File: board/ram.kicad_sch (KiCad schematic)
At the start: 8 parts, among them U1 RAM 1 LO, U5 RAM 2 LO, U6 RAM 1 LO, U7 RAM 2 LO

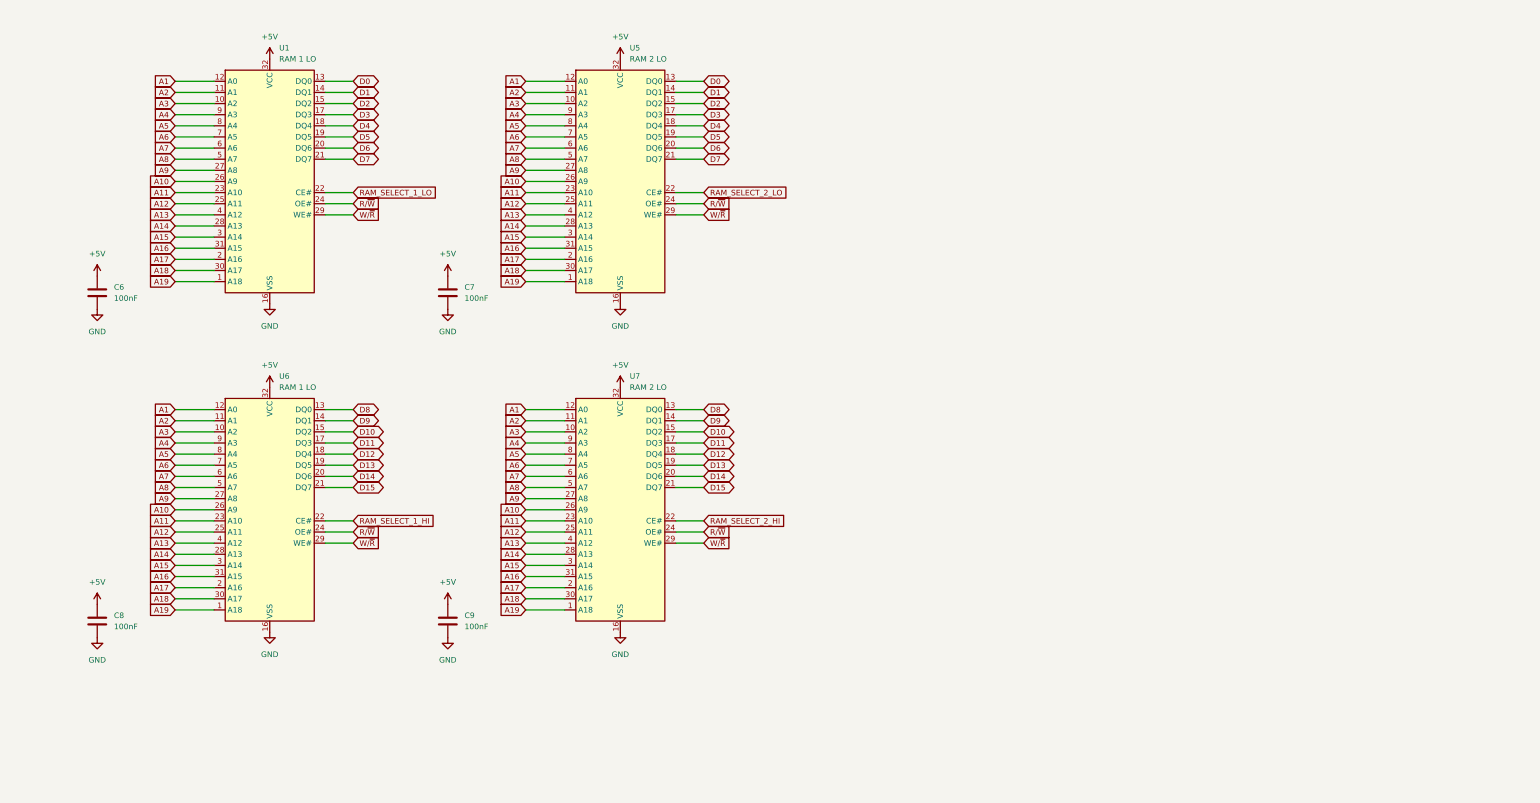
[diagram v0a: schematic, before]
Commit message: fill out most functionality - passes ERC
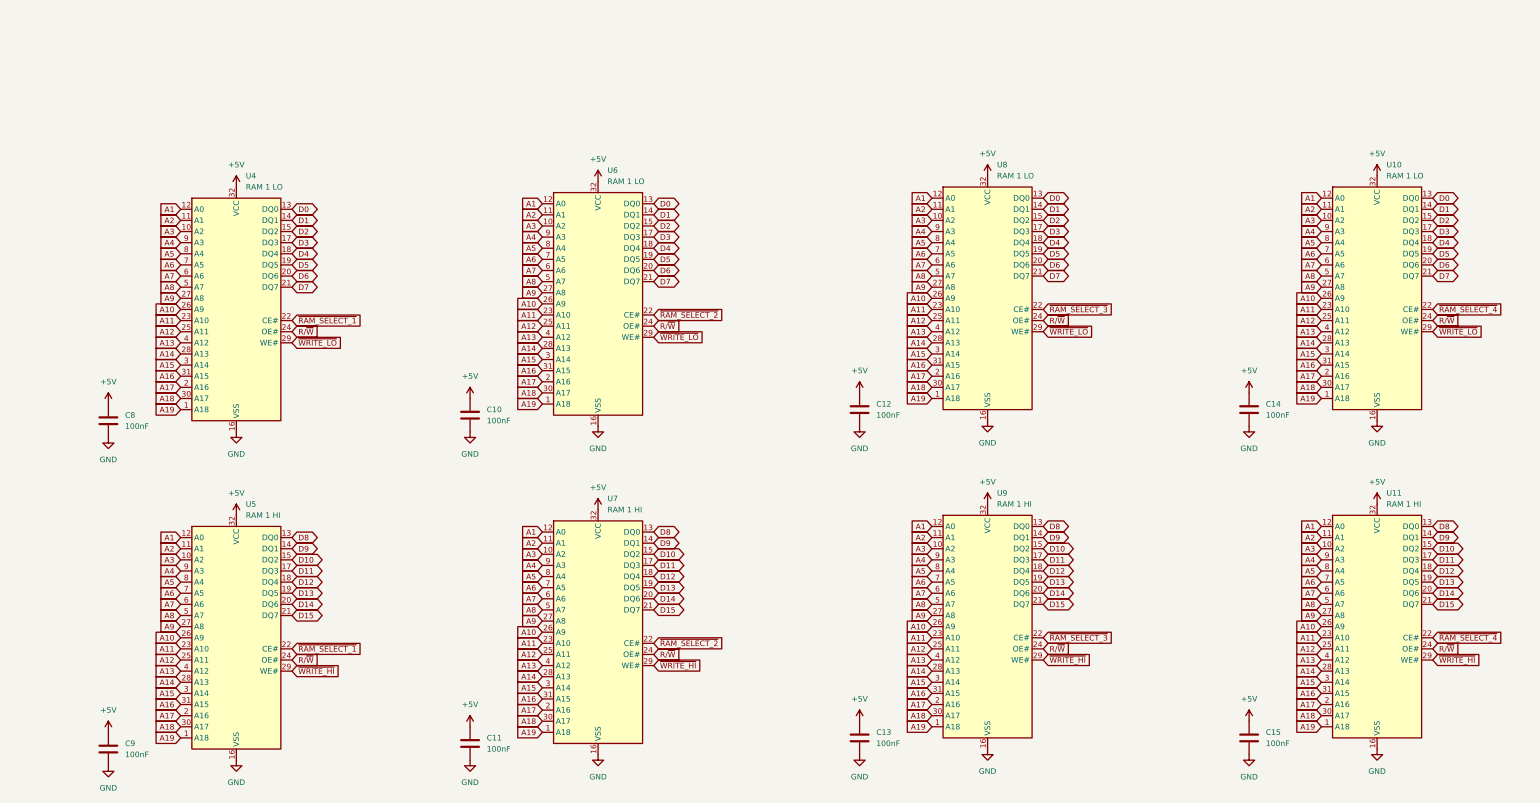
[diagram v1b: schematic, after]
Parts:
- removed C6, C7, C9: 100nF, symbol Device:C
- removed U5: RAM 2 LO, Package_DIP:DIP-32_W15.24mm, symbol Memory_RAM:AS6C4008-55PCN
- added C10, C11, C12, C13, C14, C15, C8: 100nF, symbol Device:C
- added U10, U6, U8: RAM 1 LO, Package_DIP:DIP-32_W15.24mm, symbol Memory_RAM:AS6C4008-55PCN
- added U11, U9: RAM 1 HI, Package_DIP:DIP-32_W15.24mm, symbol Memory_RAM:AS6C4008-55PCN
- U5: renamed from U6; value RAM 1 LO -> RAM 1 HI
- U7: value RAM 2 LO -> RAM 1 HI
- renumbered C8 to C9, U1 to U4
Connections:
- net RAM_SELECT_1_LO is gone; now on net ~{RAM_SELECT_1}: U4.22 (CE#)
- net +5V: now also C10.1, C11.1, C12.1, C13.1, C14.1, C15.1, C8.1, U10.32 (VCC), U11.32 (VCC), U6.32 (VCC), U8.32 (VCC), U9.32 (VCC)
- net A1: now also U10.12 (A0), U11.12 (A0), U6.12 (A0), U8.12 (A0), U9.12 (A0)
- net A10: now also U10.26 (A9), U11.26 (A9), U6.26 (A9), U8.26 (A9), U9.26 (A9)
- net A11: now also U10.23 (A10), U11.23 (A10), U6.23 (A10), U8.23 (A10), U9.23 (A10)
- net A12: now also U10.25 (A11), U11.25 (A11), U6.25 (A11), U8.25 (A11), U9.25 (A11)
- net A13: now also U10.4 (A12), U11.4 (A12), U6.4 (A12), U8.4 (A12), U9.4 (A12)
- net A14: now also U10.28 (A13), U11.28 (A13), U6.28 (A13), U8.28 (A13), U9.28 (A13)
- net A15: now also U10.3 (A14), U11.3 (A14), U6.3 (A14), U8.3 (A14), U9.3 (A14)
- net A16: now also U10.31 (A15), U11.31 (A15), U6.31 (A15), U8.31 (A15), U9.31 (A15)
- net A17: now also U10.2 (A16), U11.2 (A16), U6.2 (A16), U8.2 (A16), U9.2 (A16)
- net A18: now also U10.30 (A17), U11.30 (A17), U6.30 (A17), U8.30 (A17), U9.30 (A17)
- net A19: now also U10.1 (A18), U11.1 (A18), U6.1 (A18), U8.1 (A18), U9.1 (A18)
- net A2: now also U10.11 (A1), U11.11 (A1), U6.11 (A1), U8.11 (A1), U9.11 (A1)
- net A3: now also U10.10 (A2), U11.10 (A2), U6.10 (A2), U8.10 (A2), U9.10 (A2)
- net A4: now also U10.9 (A3), U11.9 (A3), U6.9 (A3), U8.9 (A3), U9.9 (A3)
- net A5: now also U10.8 (A4), U11.8 (A4), U6.8 (A4), U8.8 (A4), U9.8 (A4)
- net A6: now also U10.7 (A5), U11.7 (A5), U6.7 (A5), U8.7 (A5), U9.7 (A5)
- net A7: now also U10.6 (A6), U11.6 (A6), U6.6 (A6), U8.6 (A6), U9.6 (A6)
- net A8: now also U10.5 (A7), U11.5 (A7), U6.5 (A7), U8.5 (A7), U9.5 (A7)
- net A9: now also U10.27 (A8), U11.27 (A8), U6.27 (A8), U8.27 (A8), U9.27 (A8)
- net D0: now also U10.13 (DQ0), U6.13 (DQ0), U8.13 (DQ0)
- net D1: now also U10.14 (DQ1), U6.14 (DQ1), U8.14 (DQ1)
- net D10: now also U11.15 (DQ2), U9.15 (DQ2)
- net D11: now also U11.17 (DQ3), U9.17 (DQ3)
- net D12: now also U11.18 (DQ4), U9.18 (DQ4)
- net D13: now also U11.19 (DQ5), U9.19 (DQ5)
- net D14: now also U11.20 (DQ6), U9.20 (DQ6)
- net D15: now also U11.21 (DQ7), U9.21 (DQ7)
- net D2: now also U10.15 (DQ2), U6.15 (DQ2), U8.15 (DQ2)
- net D3: now also U10.17 (DQ3), U6.17 (DQ3), U8.17 (DQ3)
- net D4: now also U10.18 (DQ4), U6.18 (DQ4), U8.18 (DQ4)
- net D5: now also U10.19 (DQ5), U6.19 (DQ5), U8.19 (DQ5)
- net D6: now also U10.20 (DQ6), U6.20 (DQ6), U8.20 (DQ6)
- net D7: now also U10.21 (DQ7), U6.21 (DQ7), U8.21 (DQ7)
- net D8: now also U11.13 (DQ0), U9.13 (DQ0)
- net D9: now also U11.14 (DQ1), U9.14 (DQ1)
- net GND: now also C10.2, C11.2, C12.2, C13.2, C14.2, C15.2, C8.2, U10.16 (VSS), U11.16 (VSS), U6.16 (VSS), U8.16 (VSS), U9.16 (VSS)
- net R/~{W}: now also U10.24 (OE#), U11.24 (OE#), U6.24 (OE#), U8.24 (OE#), U9.24 (OE#)
- net RAM_SELECT_1_HI renamed ~{RAM_SELECT_1}
- net RAM_SELECT_2_HI renamed ~{RAM_SELECT_2}
- net ~{RAM_SELECT_2}: now also U6.22 (CE#)
- net W/~{R} renamed ~{WRITE_HI}
- net ~{WRITE_HI}: now also U11.29 (WE#), U9.29 (WE#); no longer U4.29 (WE#)
- new net ~{RAM_SELECT_3}: U8.22 (CE#), U9.22 (CE#)
- new net ~{RAM_SELECT_4}: U10.22 (CE#), U11.22 (CE#)
- new net ~{WRITE_LO}: U10.29 (WE#), U4.29 (WE#), U6.29 (WE#), U8.29 (WE#)
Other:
- moved on the sheet: C9, U4, U5

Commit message: design draft complete, added footprints
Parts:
- C10, C11, C12, C13, C14, C15, C8, C9: footprint (none) -> Capacitor_THT:C_Disc_D5.0mm_W2.5mm_P5.00mm
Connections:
- net R/~{W} renamed ~{R}/W
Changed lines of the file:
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@@
 		)
 	)
-	(global_label "R{slash}~{W}"
+	(global_label "~{R}{slash}W"
 		(shape input)
 		(at 250.19 165.1 0)
@@
 		)
 	)
-	(global_label "R{slash}~{W}"
+	(global_label "~{R}{slash}W"
 		(shape input)
 		(at 161.29 166.37 0)
@@
 		)
 	)
-	(global_label "R{slash}~{W}"
+	(global_label "~{R}{slash}W"
 		(shape input)
 		(at 339.09 90.17 0)
@@
 		)
 	)
-	(global_label "R{slash}~{W}"
+	(global_label "~{R}{slash}W"
 		(shape input)
 		(at 250.19 90.17 0)
@@
 		)
 	)
-	(global_label "R{slash}~{W}"
+	(global_label "~{R}{slash}W"
 		(shape input)
 		(at 161.29 91.44 0)
@@
 		)
 	)
-	(global_label "R{slash}~{W}"
+	(global_label "~{R}{slash}W"
 		(shape input)
 		(at 339.09 165.1 0)
@@
 		)
 	)
-	(global_label "R{slash}~{W}"
+	(global_label "~{R}{slash}W"
 		(shape input)
 		(at 78.74 92.71 0)
@@
 		)
 	)
-	(global_label "R{slash}~{W}"
+	(global_label "~{R}{slash}W"
 		(shape input)
 		(at 78.74 167.64 0)
@@
 			)
 		)
-		(property "Footprint" ""
+		(property "Footprint" "Capacitor_THT:C_Disc_D5.0mm_W2.5mm_P5.00mm"
 			(at 120.3452 190.5 0)
 			(effects
@@
 			)
 		)
-		(property "Footprint" ""
+		(property "Footprint" "Capacitor_THT:C_Disc_D5.0mm_W2.5mm_P5.00mm"
 			(at 298.1452 189.23 0)
 			(effects
@@
 			)
 		)
-		(property "Footprint" ""
+		(property "Footprint" "Capacitor_THT:C_Disc_D5.0mm_W2.5mm_P5.00mm"
 			(at 120.3452 115.57 0)
 			(effects
@@
 			)
 		)
-		(property "Footprint" ""
+		(property "Footprint" "Capacitor_THT:C_Disc_D5.0mm_W2.5mm_P5.00mm"
 			(at 37.7952 116.84 0)
 			(effects
@@
 			)
 		)
-		(property "Footprint" ""
+		(property "Footprint" "Capacitor_THT:C_Disc_D5.0mm_W2.5mm_P5.00mm"
 			(at 37.7952 191.77 0)
 			(effects
@@
 			)
 		)
-		(property "Footprint" ""
+		(property "Footprint" "Capacitor_THT:C_Disc_D5.0mm_W2.5mm_P5.00mm"
 			(at 298.1452 114.3 0)
 			(effects
@@
 			)
 		)
-		(property "Footprint" ""
+		(property "Footprint" "Capacitor_THT:C_Disc_D5.0mm_W2.5mm_P5.00mm"
 			(at 209.2452 189.23 0)
 			(effects
@@
 			)
 		)
-		(property "Footprint" ""
+		(property "Footprint" "Capacitor_THT:C_Disc_D5.0mm_W2.5mm_P5.00mm"
 			(at 209.2452 114.3 0)
 			(effects

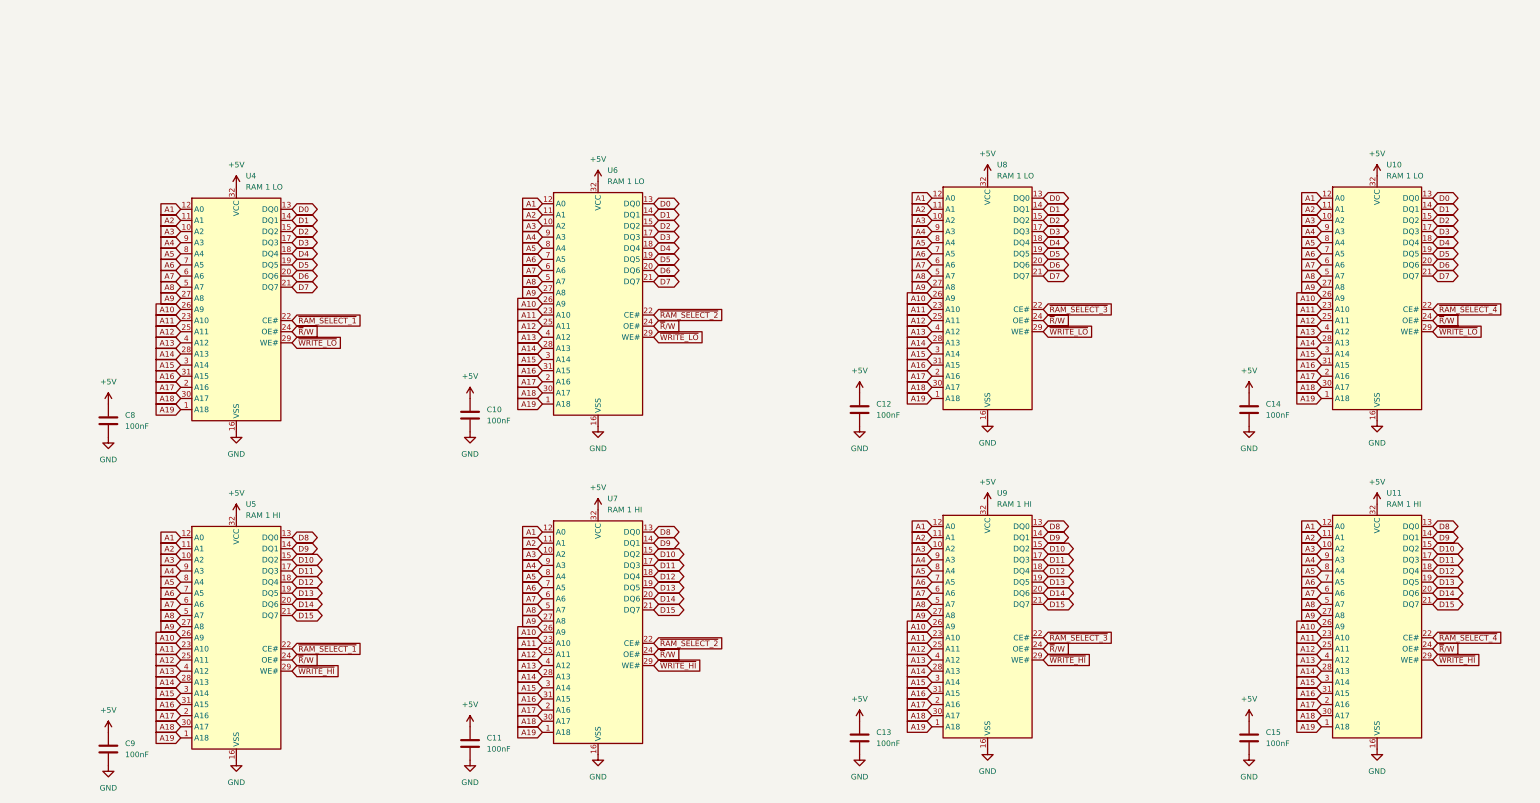
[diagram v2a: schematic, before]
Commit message: start of PCB and MMU
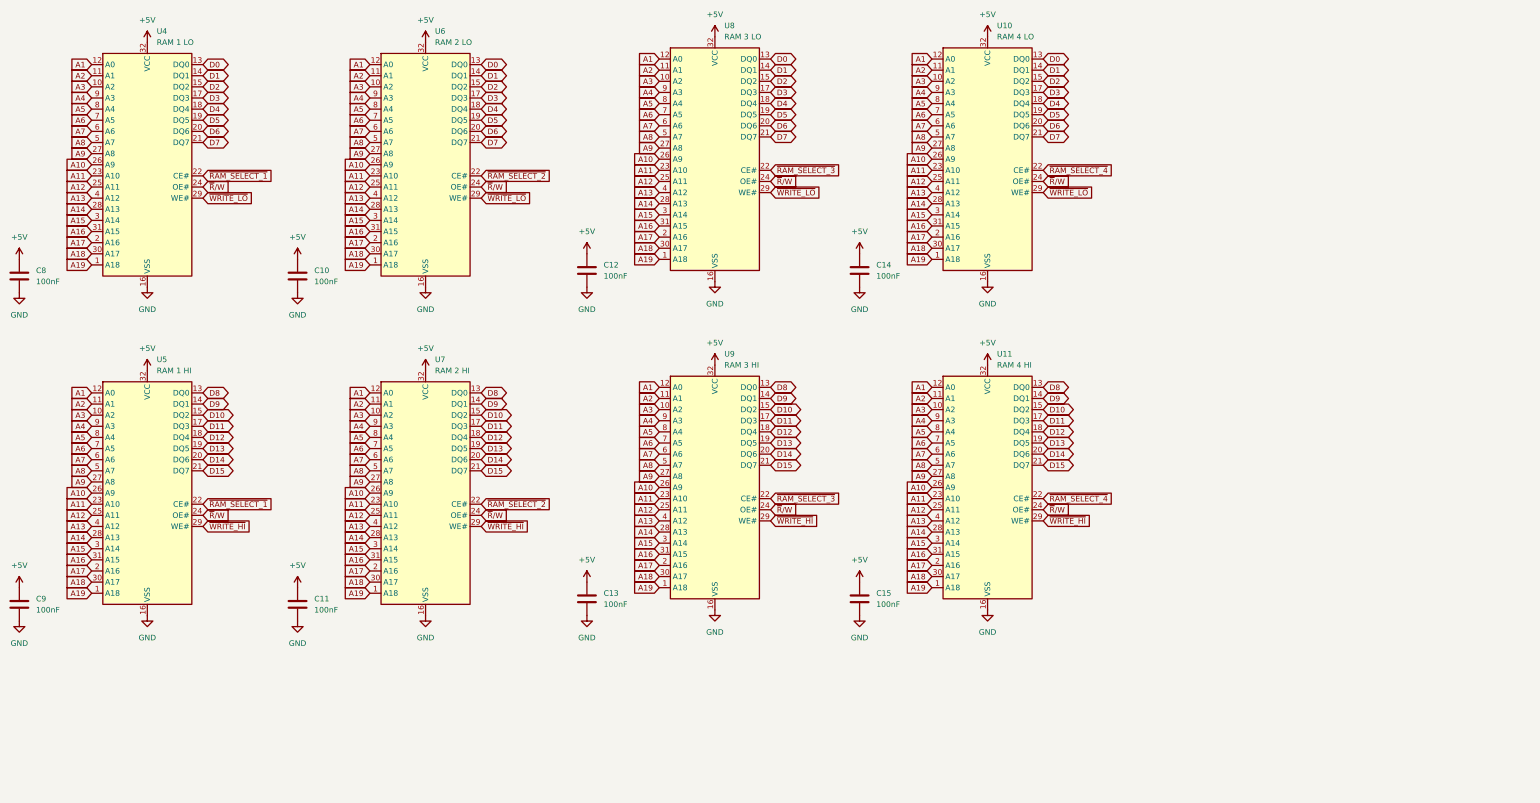
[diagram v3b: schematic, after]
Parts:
- U10: value RAM 1 LO -> RAM 4 LO
- U11: value RAM 1 HI -> RAM 4 HI
- U6: value RAM 1 LO -> RAM 2 LO
- U7: value RAM 1 HI -> RAM 2 HI
- U8: value RAM 1 LO -> RAM 3 LO
- U9: value RAM 1 HI -> RAM 3 HI
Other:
- moved on the sheet: C10, C11, C12, C13, C14, C15, C8, C9, U10, U11, U4, U5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

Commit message: checkpoint
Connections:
- net ~{R}/W is gone; now on net GND: U10.24 (OE#), U11.24 (OE#), U4.24 (OE#), U5.24 (OE#), U6.24 (OE#), U7.24 (OE#), U8.24 (OE#), U9.24 (OE#)
